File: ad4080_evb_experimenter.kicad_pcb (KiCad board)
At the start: 4 copper layers, 104.4 x 78.7 mm, 62 parts, among them J1 Conn_Coaxial, J2 Conn_Coaxial, J3 AudioJack2_Ground, J4 Conn_02x01, J5 Conn_02x01, J6 Conn_Coaxial, SW1 SW_Coded_SH-7050, U2 74LS163, U3 74HC04, X1 CXO_DIP8

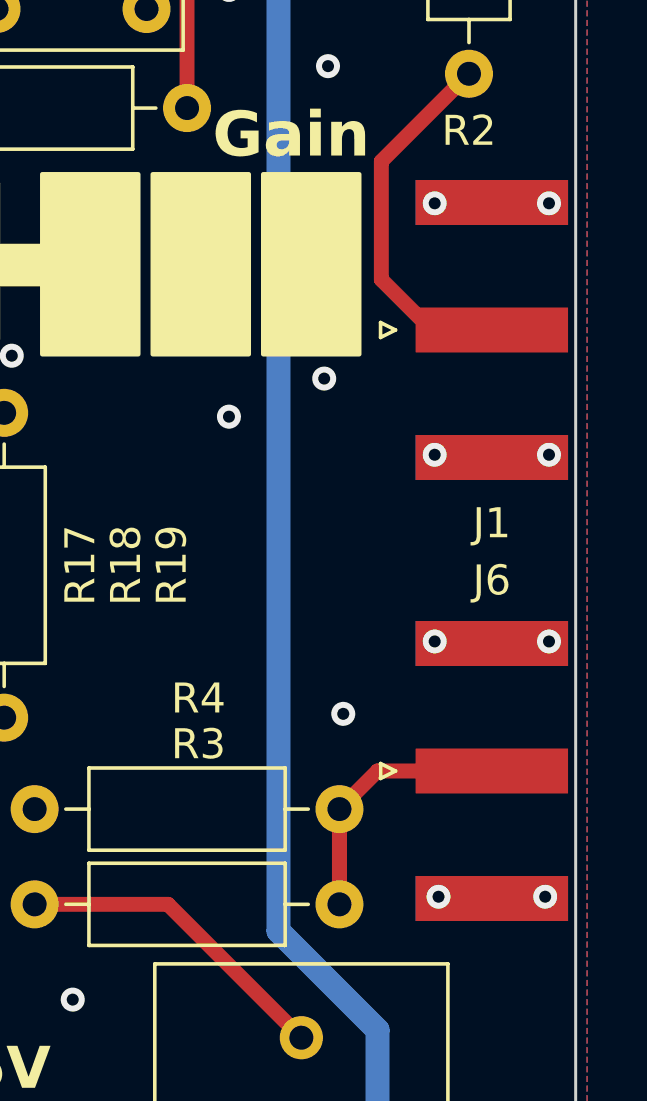
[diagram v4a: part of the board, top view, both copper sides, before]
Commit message: Set correct 14mm output SMA spacing
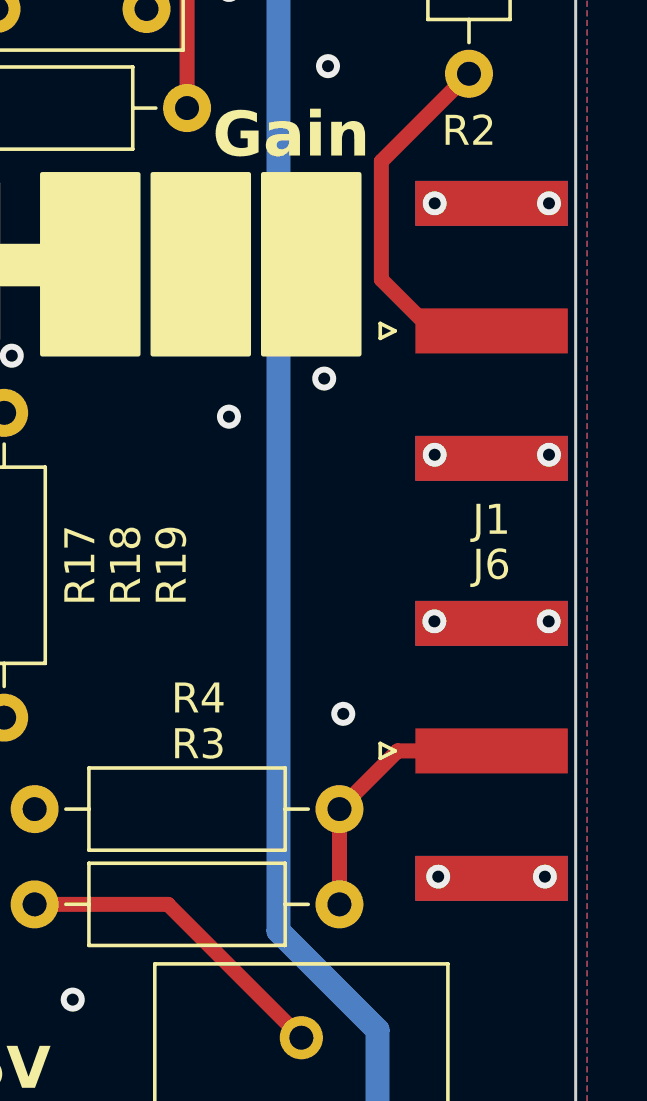
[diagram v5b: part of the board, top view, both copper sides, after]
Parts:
- moved J6 0.67 mm to (130.8, 102.2)
